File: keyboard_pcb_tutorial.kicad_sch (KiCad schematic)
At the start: 24 parts, among them SW1 SW_Push, U1 ATmega32U4-A, Y1 16MHz

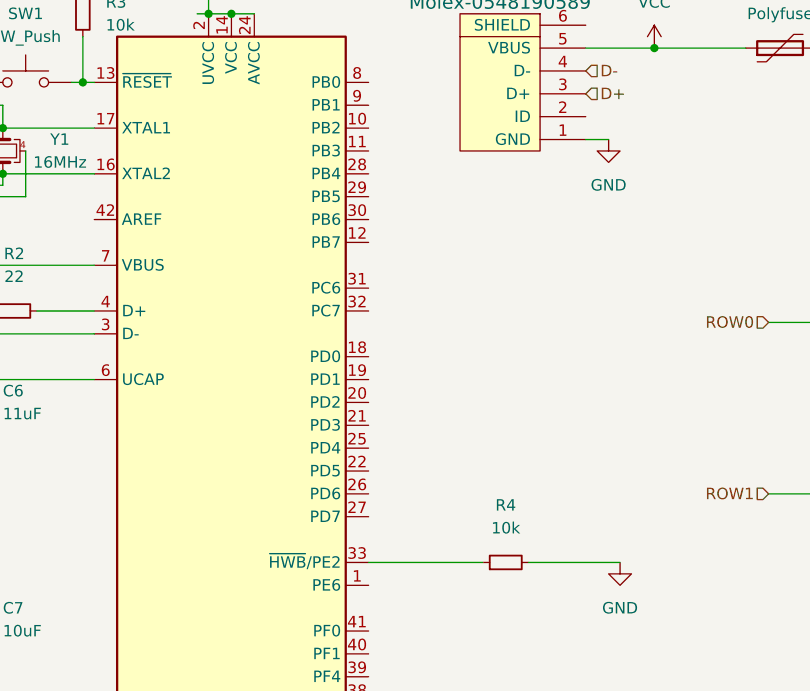
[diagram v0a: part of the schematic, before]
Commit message: PCB Component Positioning and Routing
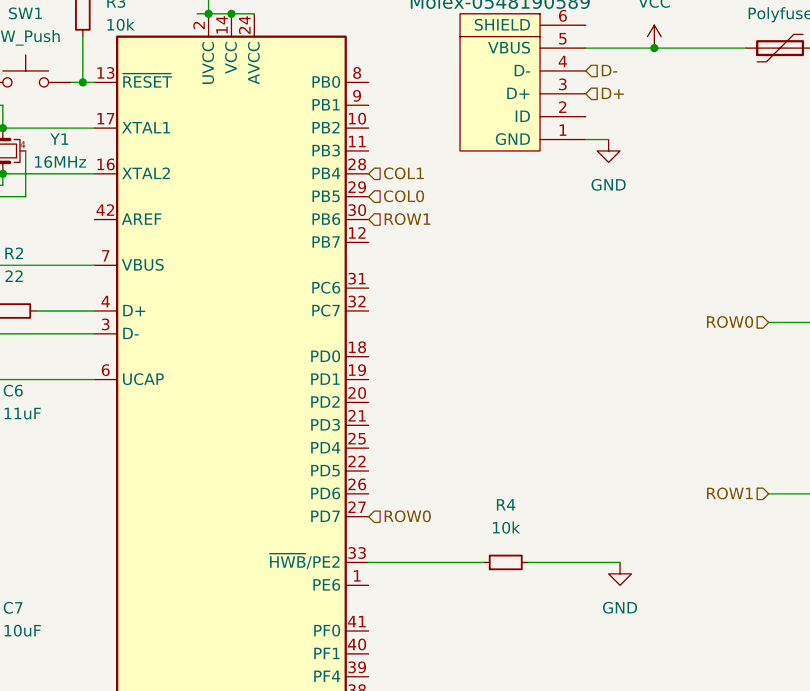
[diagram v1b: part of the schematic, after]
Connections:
- net COL0: now also U1.29 (PB5)
- net COL1: now also U1.28 (PB4)
- net ROW0: now also U1.27 (PD7)
- net ROW1: now also U1.30 (PB6)
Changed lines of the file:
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@@
     (stroke (width 0) (type default) (color 0 0 0 0))
+  )
+  (hierarchical_label "COL0" (shape input) (at 121.92 69.85 0)
+    (effects (font (size 1.27 1.27)) (justify left))
+  )
+  (hierarchical_label "COL1" (shape input) (at 121.92 67.31 0)
+    (effects (font (size 1.27 1.27)) (justify left))
   )
   (hierarchical_label "ROW0" (shape input) (at 166.37 83.82 180)
@@
   )
   (hierarchical_label "D+" (shape input) (at 146.05 58.42 0)
+    (effects (font (size 1.27 1.27)) (justify left))
+  )
+  (hierarchical_label "ROW1" (shape input) (at 121.92 72.39 0)
     (effects (font (size 1.27 1.27)) (justify left))
   )
@@
     (effects (font (size 1.27 1.27)) (justify right))
   )
+  (hierarchical_label "ROW0" (shape input) (at 121.92 105.41 0)
+    (effects (font (size 1.27 1.27)) (justify left))
+  )
   (symbol (lib_id "Device:D_Small") (at 194.31 81.28 90) (unit 1)
